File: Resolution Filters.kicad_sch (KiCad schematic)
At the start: 25 parts, among them J501 Conn_Coaxial, J502 Conn_Coaxial

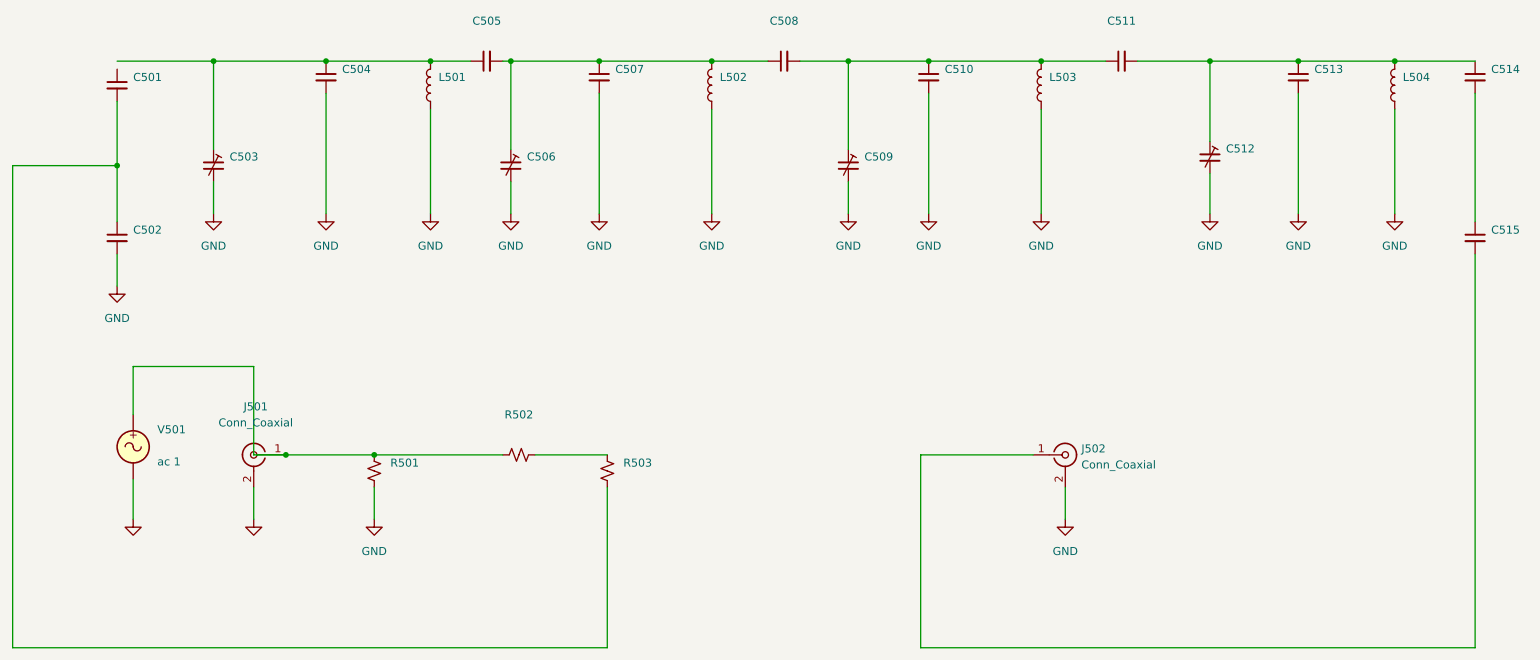
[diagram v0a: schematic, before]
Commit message: Reduced size of timebase pcb
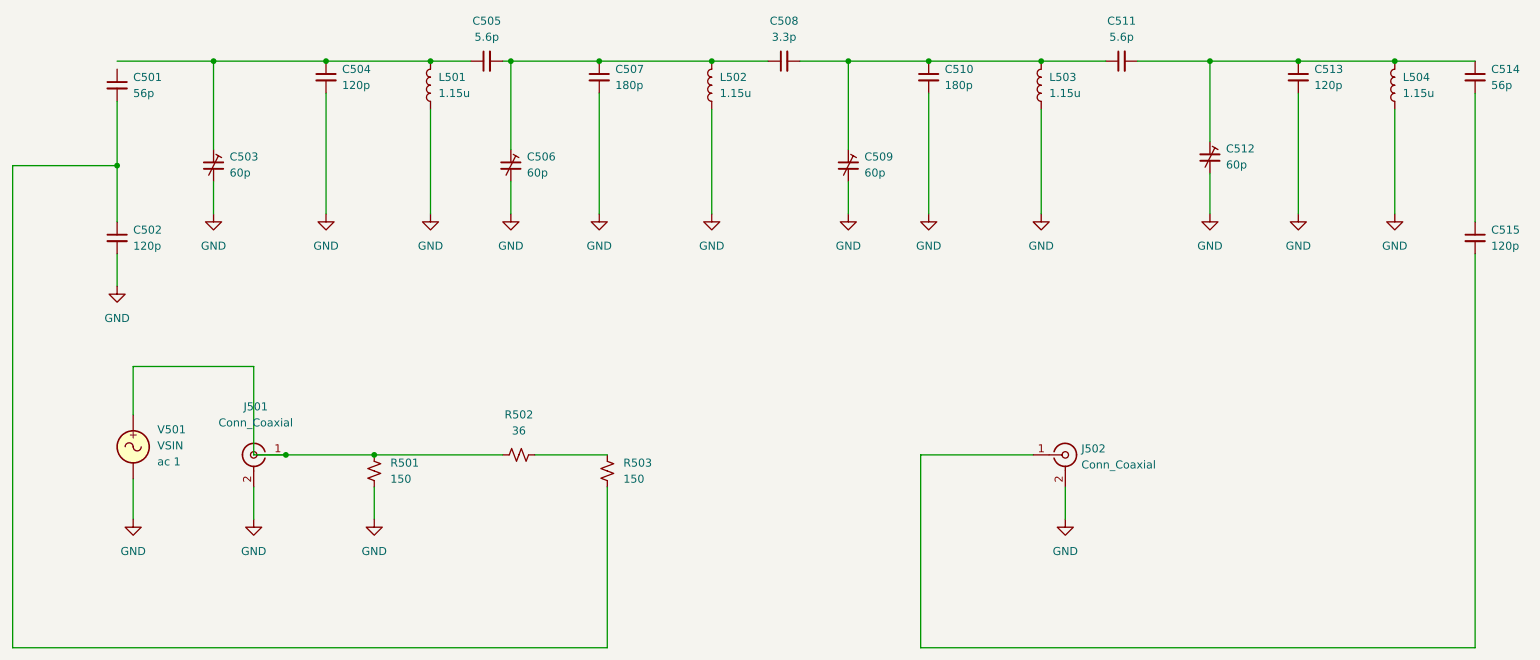
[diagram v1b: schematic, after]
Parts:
- C501, C514: value (none) -> 56p
- C502, C504, C513, C515: value (none) -> 120p
- C503, C506, C509, C512: value (none) -> 60p
- C505, C511: value (none) -> 5.6p
- C507, C510: value (none) -> 180p
- C508: value (none) -> 3.3p
- L501, L502, L503, L504: value (none) -> 1.15u
- R501, R503: value (none) -> 150
- R502: value (none) -> 36
- V501: value (none) -> VSIN
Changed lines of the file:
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@@
       (effects (font (size 1.27 1.27)) (justify left))
     )
-    (property "Value" "" (id 1) (at 106.68 116.8399 0)
+    (property "Value" "150" (id 1) (at 106.68 116.8399 0)
       (effects (font (size 1.27 1.27)) (justify left))
     )
@@
       (effects (font (size 1.27 1.27)) (justify left))
     )
-    (property "Value" "" (id 1) (at 194.31 54.6162 0)
+    (property "Value" "180p" (id 1) (at 194.31 54.6162 0)
       (effects (font (size 1.27 1.27)) (justify left))
     )
@@
       (effects (font (size 1.27 1.27)) (justify left))
     )
-    (property "Value" "" (id 1) (at 69.85 111.5701 0)
+    (property "Value" "VSIN" (id 1) (at 69.85 111.5701 0)
       (effects (font (size 1.27 1.27)) (justify left))
     )
@@
       (effects (font (size 1.27 1.27)) (justify right))
     )
-    (property "Value" "" (id 1) (at 158.75 55.8799 0)
+    (property "Value" "1.15u" (id 1) (at 158.75 55.8799 0)
       (effects (font (size 1.27 1.27)) (justify right))
     )
@@
       (effects (font (size 1.27 1.27)) (justify left))
     )
-    (property "Value" "" (id 1) (at 238.76 67.1829 0)
+    (property "Value" "60p" (id 1) (at 238.76 67.1829 0)
       (effects (font (size 1.27 1.27)) (justify left))
     )
@@
       (effects (font (size 1.27 1.27)) (justify left))
     )
-    (property "Value" "" (id 1) (at 252.73 54.6162 0)
+    (property "Value" "120p" (id 1) (at 252.73 54.6162 0)
       (effects (font (size 1.27 1.27)) (justify left))
     )
@@
     (in_bom yes) (on_board yes) (fields_autoplaced)
     (property "Reference" "R502" (id 0) (at 127 106.68 90))
-    (property "Value" "" (id 1) (at 127 109.22 90))
+    (property "Value" "36" (id 1) (at 127 109.22 90))
     (property "Footprint" "" (id 2) (at 127 113.03 0)
       (effects (font (size 1.27 1.27)) hide)
@@
       (effects (font (size 1.27 1.27)) (justify left))
     )
-    (property "Value" "" (id 1) (at 99.06 54.6162 0)
+    (property "Value" "120p" (id 1) (at 99.06 54.6162 0)
       (effects (font (size 1.27 1.27)) (justify left))
     )
@@
     (in_bom yes) (on_board yes) (fields_autoplaced)
     (property "Reference" "C511" (id 0) (at 222.2563 44.45 90))
-    (property "Value" "" (id 1) (at 222.2563 46.99 90))
+    (property "Value" "5.6p" (id 1) (at 222.2563 46.99 90))
     (property "Footprint" "" (id 2) (at 222.25 50.8 0)
       (effects (font (size 1.27 1.27)) hide)
@@
       (effects (font (size 1.27 1.27)) (justify left))
     )
-    (property "Value" "" (id 1) (at 280.67 54.6162 0)
+    (property "Value" "56p" (id 1) (at 280.67 54.6162 0)
       (effects (font (size 1.27 1.27)) (justify left))
     )
@@
       (effects (font (size 1.27 1.27)) (justify left))
     )
-    (property "Value" "" (id 1) (at 66.04 80.0162 0)
+    (property "Value" "120p" (id 1) (at 66.04 80.0162 0)
       (effects (font (size 1.27 1.27)) (justify left))
     )
@@
       (effects (font (size 1.27 1.27)) hide)
     )
-    (property "Value" "" (id 1) (at 85.09 128.27 0))
+    (property "Value" "GND" (id 1) (at 85.09 128.27 0))
     (property "Footprint" "" (id 2) (at 85.09 123.19 0)
       (effects (font (size 1.27 1.27)) hide)
@@
     (in_bom yes) (on_board yes) (fields_autoplaced)
     (property "Reference" "C508" (id 0) (at 168.9163 44.45 90))
-    (property "Value" "" (id 1) (at 168.9163 46.99 90))
+    (property "Value" "3.3p" (id 1) (at 168.9163 46.99 90))
     (property "Footprint" "" (id 2) (at 168.91 50.8 0)
       (effects (font (size 1.27 1.27)) hide)
@@
       (effects (font (size 1.27 1.27)) hide)
     )
-    (property "Value" "" (id 1) (at 66.04 128.27 0))
+    (property "Value" "GND" (id 1) (at 66.04 128.27 0))
     (property "Footprint" "" (id 2) (at 66.04 123.19 0)
       (effects (font (size 1.27 1.27)) hide)
@@
       (effects (font (size 1.27 1.27)) (justify right))
     )
-    (property "Value" "" (id 1) (at 114.3 55.8799 0)
+    (property "Value" "1.15u" (id 1) (at 114.3 55.8799 0)
       (effects (font (size 1.27 1.27)) (justify right))
     )
@@
       (effects (font (size 1.27 1.27)) (justify left))
     )
-    (property "Value" "" (id 1) (at 81.28 68.4529 0)
+    (property "Value" "60p" (id 1) (at 81.28 68.4529 0)
       (effects (font (size 1.27 1.27)) (justify left))
     )
@@
       (effects (font (size 1.27 1.27)) (justify left))
     )
-    (property "Value" "" (id 1) (at 128.27 68.4529 0)
+    (property "Value" "60p" (id 1) (at 128.27 68.4529 0)
       (effects (font (size 1.27 1.27)) (justify left))
     )
@@
       (effects (font (size 1.27 1.27)) (justify right))
     )
-    (property "Value" "" (id 1) (at 266.7 55.8799 0)
+    (property "Value" "1.15u" (id 1) (at 266.7 55.8799 0)
       (effects (font (size 1.27 1.27)) (justify right))
     )
@@
       (effects (font (size 1.27 1.27)) (justify left))
     )
-    (property "Value" "" (id 1) (at 142.24 54.6162 0)
+    (property "Value" "180p" (id 1) (at 142.24 54.6162 0)
       (effects (font (size 1.27 1.27)) (justify left))
     )
@@
     (in_bom yes) (on_board yes) (fields_autoplaced)
     (property "Reference" "C505" (id 0) (at 121.9263 44.45 90))
-    (property "Value" "" (id 1) (at 121.9263 46.99 90))
+    (property "Value" "5.6p" (id 1) (at 121.9263 46.99 90))
     (property "Footprint" "" (id 2) (at 121.92 50.8 0)
       (effects (font (size 1.27 1.27)) hide)
@@
       (effects (font (size 1.27 1.27)) (justify left))
     )
-    (property "Value" "" (id 1) (at 143.51 116.8399 0)
+    (property "Value" "150" (id 1) (at 143.51 116.8399 0)
       (effects (font (size 1.27 1.27)) (justify left))
     )
@@
       (effects (font (size 1.27 1.27)) (justify right))
     )
-    (property "Value" "" (id 1) (at 210.82 55.8799 0)
+    (property "Value" "1.15u" (id 1) (at 210.82 55.8799 0)
       (effects (font (size 1.27 1.27)) (justify right))
     )
@@
       (effects (font (size 1.27 1.27)) (justify left))
     )
-    (property "Value" "" (id 1) (at 181.61 68.4529 0)
+    (property "Value" "60p" (id 1) (at 181.61 68.4529 0)
       (effects (font (size 1.27 1.27)) (justify left))
     )
@@
       (effects (font (size 1.27 1.27)) (justify left))
     )
-    (property "Value" "" (id 1) (at 66.04 55.8862 0)
+    (property "Value" "56p" (id 1) (at 66.04 55.8862 0)
       (effects (font (size 1.27 1.27)) (justify left))
     )
@@
       (effects (font (size 1.27 1.27)) (justify left))
     )
-    (property "Value" "" (id 1) (at 280.67 80.0162 0)
-      (effects (font (size 1.27 1.27)) (justify left))
-    )
+    (property "Value" "120p" (id 1) (at 280.67 80.0162 0)
+      (effects (font (size 1.27 1.27)) (justify left))
+    )

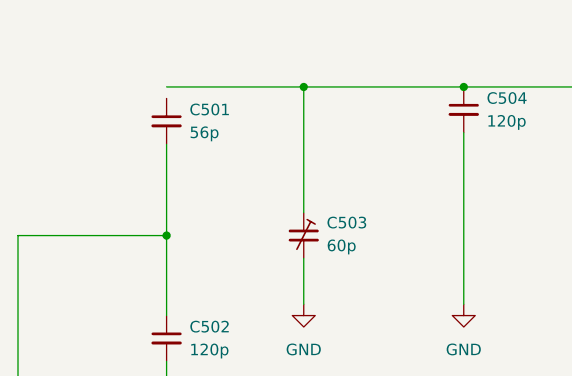
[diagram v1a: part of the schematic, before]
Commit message: Significant changes to timebase spice, 15v supply and resolution-filters
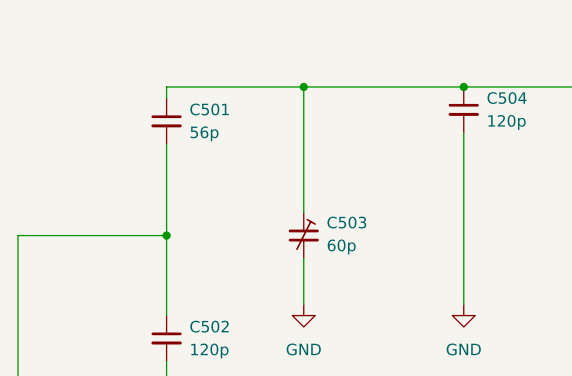
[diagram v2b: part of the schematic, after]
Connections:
- net at C503.1, C504.1, C505.1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: now also C501.1
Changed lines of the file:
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@@
+    (stroke (width 0) (type default) (color 0 0 0 0))
+  )
+  (wire (pts (xy 63.5 52.07) (xy 63.5 50.8))
     (stroke (width 0) (type default) (color 0 0 0 0))
   )
